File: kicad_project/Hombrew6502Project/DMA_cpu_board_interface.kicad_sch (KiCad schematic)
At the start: 19 parts, among them J601 DMA_CTRL, J602 DMA_CTRL, J603 DATA, ADDR, J604 DATA, ADDR, U106 SN74LS07, U508 74AHC2G32DP, U509 74AHC2G32DP

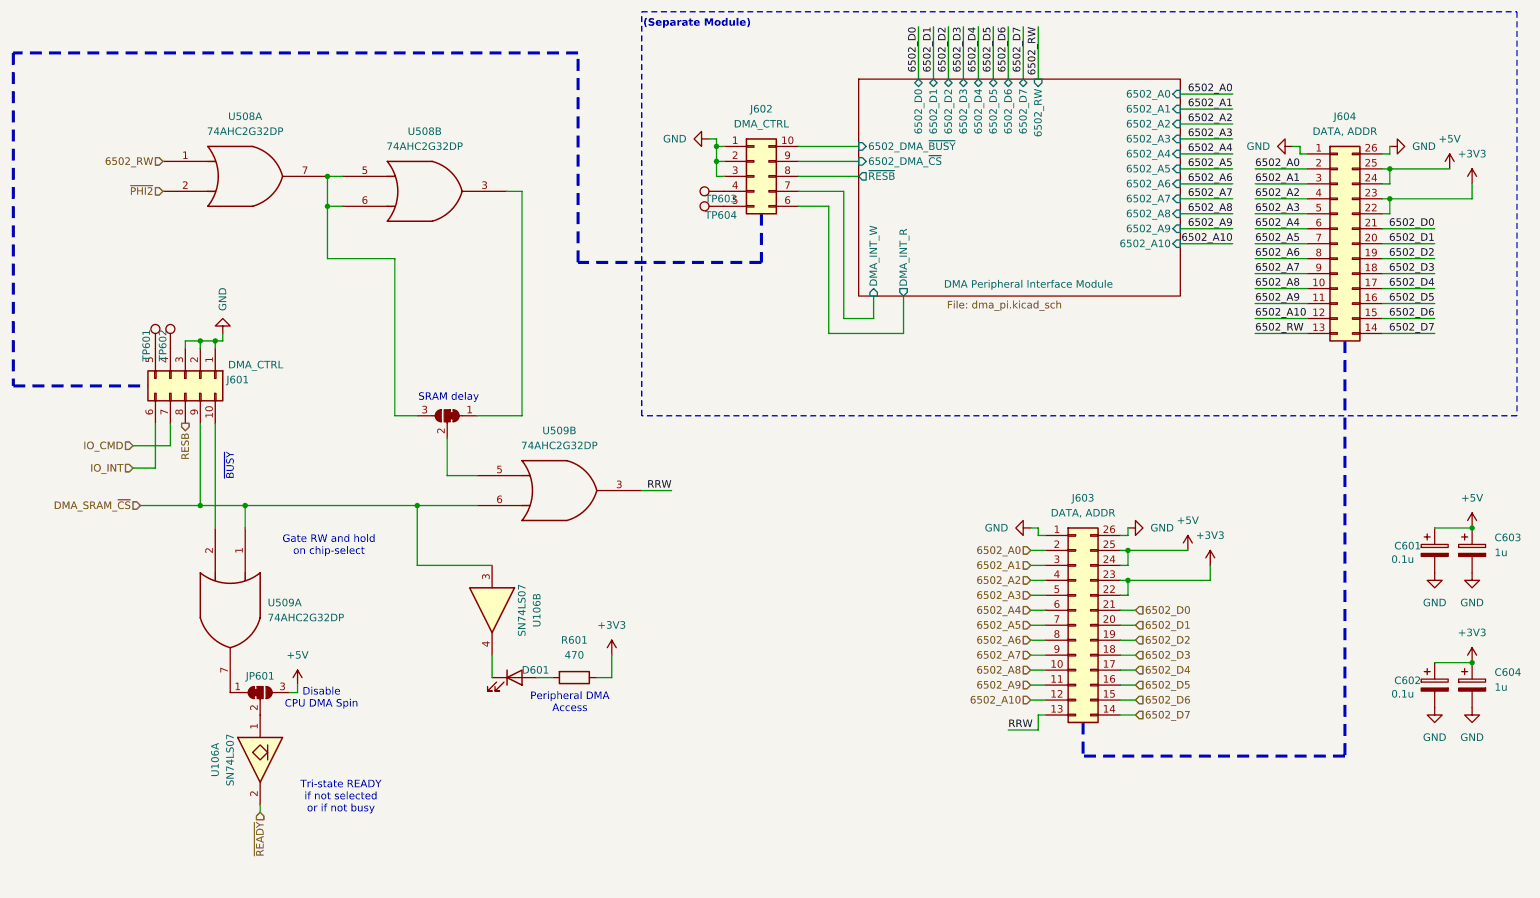
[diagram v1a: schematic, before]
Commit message: Made DMA peripheral stuff on same board
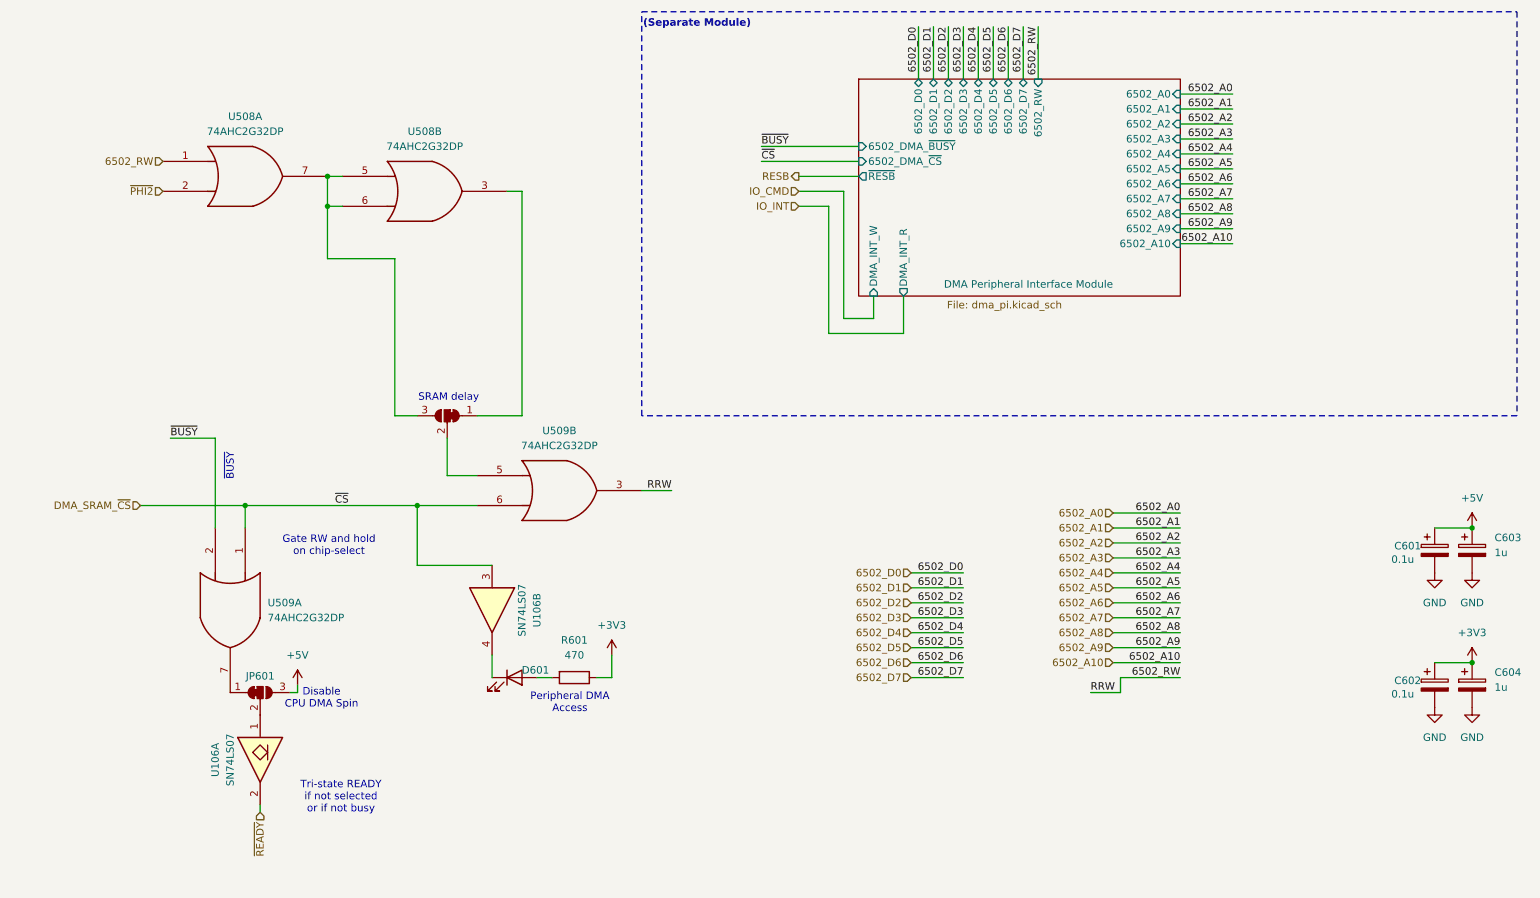
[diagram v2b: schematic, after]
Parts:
- removed J601, J602: DMA_CTRL, symbol Connector_Generic:Conn_02x05_Counter_Clockwise
- removed J603, J604: DATA, ADDR, symbol Connector_Generic:Conn_02x13_Counter_Clockwise
- removed TP601, TP602, TP603, TP604: TestPoint, TestPoint:TestPoint_Pad_D1.5mm, symbol Connector:TestPoint
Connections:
- net RRW is gone; now on net 6502_RW: U509.3
- net ~{BUSY}: now reaches U509.2

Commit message: Layout mostly finished
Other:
- note removed: "(Separate Module)"
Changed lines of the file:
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@@
 	(title_block
 		(title "65c02 Homebrew")
-		(rev "Prelim")
+		(rev "Rev A")
 		(company "Joseph R. Freeston")
 		(comment 2 "https://github.com/snorklerjoe/useful6502")
 		(comment 4 "A 65c02-based computer with peripheral i/o offloaded to a PIC16 microcontroller.")
-	)
-	(rectangle
-		(start 127 31.75)
-		(end 275.59 100.33)
-		(stroke
-			(width 0)
-			(type dash_dot_dot)
-		)
-		(fill
-			(type none)
-		)
 	)
 	(text "SRAM delay"
@@
 			)
 		)
-	)
-	(text "(Separate Module)"
-		(exclude_from_sim no)
-		(at 136.398 33.782 0)
-		(effects
-			(font
-				(size 1.27 1.27)
-				(thickness 0.254)
-				(bold yes)
-			)
-		)
